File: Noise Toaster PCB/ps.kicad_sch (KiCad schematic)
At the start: 8 parts

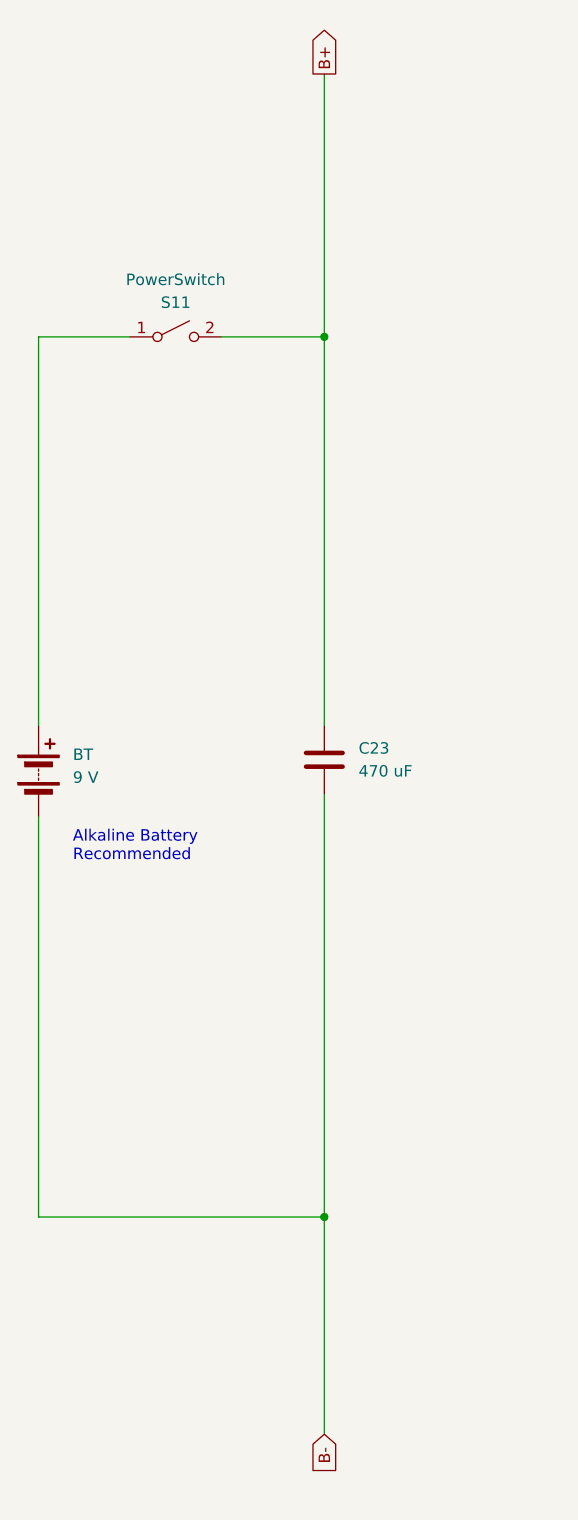
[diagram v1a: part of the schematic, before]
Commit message: refactored the schematic
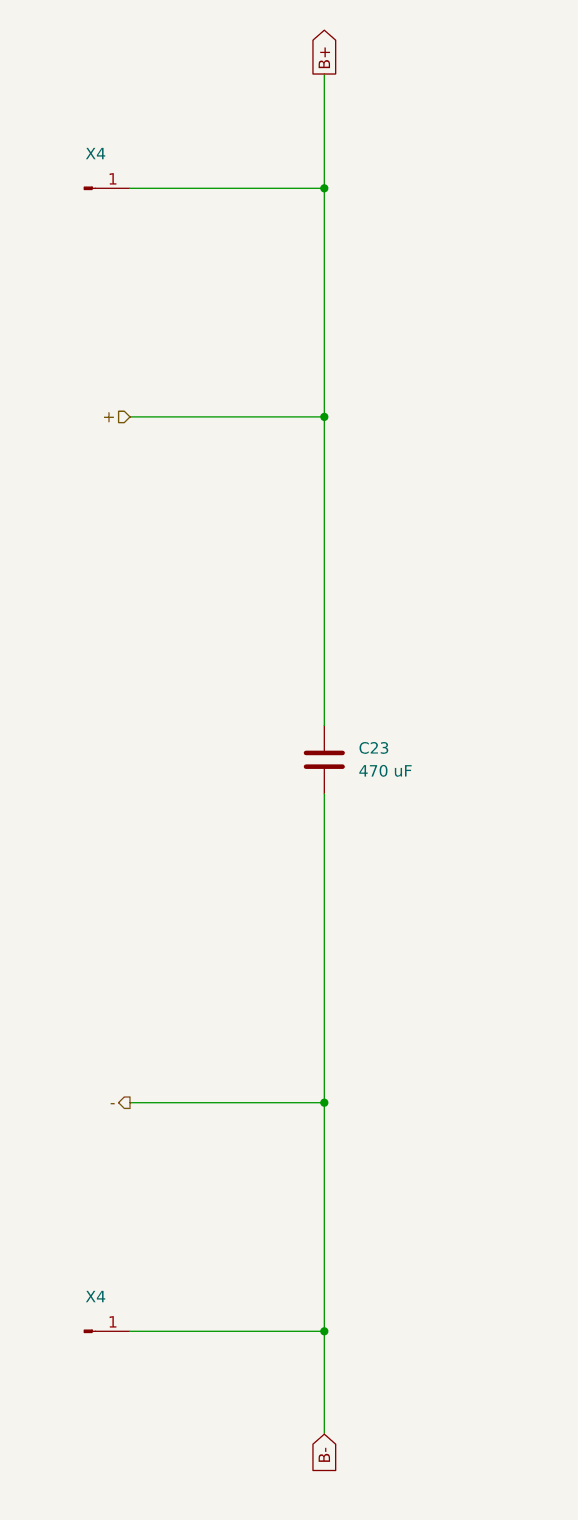
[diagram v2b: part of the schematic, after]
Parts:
- removed BT: 9 V, symbol Device:Battery
- removed PowerSwitch: S11, symbol Switch:SW_SPST
- added X4 (x2): ~, symbol Connector:Conn_01x01_Pin
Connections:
- net B+: now also X4.1 (Pin_1)
- net B-: now also X4.1 (Pin_1)
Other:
- note removed: "Alkaline Battery Recommended"
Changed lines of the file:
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@@
     (comment 3 "Music From Outer Space LLC")
   )
-  (junction (at 59.69 54.61) (diameter 0) (color 0 0 0 0)
+  (junction (at 59.69 139.7) (diameter 0) (color 0 0 0 0)
+  )
+  (junction (at 59.69 165.1) (diameter 0) (color 0 0 0 0)
   )
   (junction (at 160.02 105.41) (diameter 0) (color 0 0 0 0)
@@
   (junction (at 160.02 63.5) (diameter 0) (color 0 0 0 0)
   )
-  (junction (at 59.69 152.4) (diameter 0) (color 0 0 0 0)
+  (junction (at 59.69 63.5) (diameter 0) (color 0 0 0 0)
+  )
+  (junction (at 59.69 38.1) (diameter 0) (color 0 0 0 0)
   )
   (junction (at 105.41 104.14) (diameter 0) (color 0 0 0 0)
   )
-  (wire (pts (xy 59.69 152.4) (xy 59.69 176.53))
+  (wire (pts (xy 38.1 139.7) (xy 59.69 139.7))
+    (stroke (width 0) (type default))
+  )
+  (wire (pts (xy 59.69 38.1) (xy 59.69 63.5))
+    (stroke (width 0) (type default))
+  )
+  (wire (pts (xy 59.69 105.41) (xy 59.69 139.7))
+    (stroke (width 0) (type default))
+  )
+  (wire (pts (xy 38.1 38.1) (xy 59.69 38.1))
     (stroke (width 0) (type default))
   )
@@
     (stroke (width 0) (type default))
   )
-  (wire (pts (xy 27.94 54.61) (xy 27.94 97.79))
-    (stroke (width 0) (type default))
-  )
   (wire (pts (xy 223.52 76.2) (xy 223.52 63.5))
     (stroke (width 0) (type default))
@@
     (stroke (width 0) (type default))
   )
+  (wire (pts (xy 38.1 63.5) (xy 59.69 63.5))
+    (stroke (width 0) (type default))
+  )
   (wire (pts (xy 160.02 26.67) (xy 160.02 41.91))
     (stroke (width 0) (type default))
   )
+  (wire (pts (xy 59.69 63.5) (xy 59.69 97.79))
+    (stroke (width 0) (type default))
+  )
   (wire (pts (xy 105.41 83.82) (xy 105.41 104.14))
     (stroke (width 0) (type default))
@@
     (stroke (width 0) (type default))
   )
-  (wire (pts (xy 27.94 54.61) (xy 38.1 54.61))
-    (stroke (width 0) (type default))
-  )
-  (wire (pts (xy 59.69 54.61) (xy 59.69 97.79))
+  (wire (pts (xy 59.69 165.1) (xy 59.69 176.53))
     (stroke (width 0) (type default))
   )
@@
     (stroke (width 0) (type default))
   )
+  (wire (pts (xy 59.69 139.7) (xy 59.69 165.1))
+    (stroke (width 0) (type default))
+  )
   (wire (pts (xy 120.65 106.68) (xy 120.65 104.14))
     (stroke (width 0) (type default))
@@
     (stroke (width 0) (type default))
   )
-  (wire (pts (xy 27.94 107.95) (xy 27.94 152.4))
-    (stroke (width 0) (type default))
-  )
   (wire (pts (xy 160.02 63.5) (xy 160.02 105.41))
     (stroke (width 0) (type default))
   )
-  (wire (pts (xy 27.94 152.4) (xy 59.69 152.4))
-    (stroke (width 0) (type default))
-  )
-  (wire (pts (xy 59.69 25.4) (xy 59.69 54.61))
+  (wire (pts (xy 38.1 165.1) (xy 59.69 165.1))
+    (stroke (width 0) (type default))
+  )
+  (wire (pts (xy 59.69 25.4) (xy 59.69 38.1))
     (stroke (width 0) (type default))
   )
@@
     (stroke (width 0) (type default))
   )
-  (wire (pts (xy 59.69 152.4) (xy 59.69 105.41))
-    (stroke (width 0) (type default))
-  )
   (wire (pts (xy 105.41 104.14) (xy 120.65 104.14))
-    (stroke (width 0) (type default))
-  )
-  (wire (pts (xy 48.26 54.61) (xy 59.69 54.61))
     (stroke (width 0) (type default))
   )
   (text "Current Drain is\nbetween 15 to \n20 mA. More if\nused at high\noutput levels."
     (at 180.34 88.9 0)
-    (effects (font (size 1.27 1.27)) (justify left bottom))
-  )
-  (text "Alkaline Battery\nRecommended" (at 31.75 113.03 0)
     (effects (font (size 1.27 1.27)) (justify left bottom))
   )
@@
     )
   )
-  (symbol (lib_id "Switch:SW_SPST") (at 43.18 54.61 0) (unit 1)
-    (in_bom yes) (on_board yes) (dnp no) (fields_autoplaced)
-    (property "Reference" "PowerSwitch" (at 43.18 48.26 0)
-      (effects (font (size 1.27 1.27)))
-    )
-    (property "Value" "S11" (at 43.18 50.8 0)
-      (effects (font (size 1.27 1.27)))
-    )
-    (property "Footprint" "" (at 43.18 54.61 0)
-      (effects (font (size 1.27 1.27)) hide)
-    )
-    (property "Datasheet" "~" (at 43.18 54.61 0)
-      (effects (font (size 1.27 1.27)) hide)
-    )
-    (pin "1")
-    (pin "2")
-    (instances
-      (project "Noise Toaster PCB"
-        (path "/7be3f398-d902-4566-9ee4-0bff072cd47e/8163954c-0389-42ef-b929-449d078595e3"
-          (reference "PowerSwitch") (unit 1)
+  (hierarchical_label "-" (shape output) (at 38.1 139.7 180) (fields_autoplaced)
+    (effects (font (size 1.27 1.27)) (justify right))
+  )
+  (hierarchical_label "+" (shape input) (at 38.1 63.5 180) (fields_autoplaced)
+    (effects (font (size 1.27 1.27)) (justify right))
+  )
+  (symbol (lib_id "Connector:Conn_01x01_Pin") (at 33.02 38.1 0) (unit 1)
+    (in_bom yes) (on_board yes) (dnp no)
+    (property "Reference" "X4" (at 34.29 34.29 0)
+      (effects (font (size 1.27 1.27)))
+    )
+    (property "Value" "~" (at 33.655 35.56 0)
+      (effects (font (size 1.27 1.27)))
+    )
+    (property "Footprint" "" (at 33.02 38.1 0)
+      (effects (font (size 1.27 1.27)) hide)
+    )
+    (property "Datasheet" "~" (at 33.02 38.1 0)
+      (effects (font (size 1.27 1.27)) hide)
+    )
+    (pin "1")
+    (instances
+      (project "Noise Toaster PCB"
+        (path "/7be3f398-d902-4566-9ee4-0bff072cd47e/818b46cb-815d-4132-b52d-9731333b7f1f"
+          (reference "X4") (unit 1)
+        )
+        (path "/7be3f398-d902-4566-9ee4-0bff072cd47e/d0369b76-3398-4137-86ba-22490a5aca99"
+          (reference "X21") (unit 1)
+        )
+        (path "/7be3f398-d902-4566-9ee4-0bff072cd47e/0647ade8-e724-4924-aa52-6cbb42374298"
+          (reference "X21") (unit 1)
+        )
+        (path "/7be3f398-d902-4566-9ee4-0bff072cd47e/8163954c-0389-42ef-b929-449d078595e3"
+          (reference "B+") (unit 1)
+        )
+      )
+    )
+  )
+  (symbol (lib_id "Connector:Conn_01x01_Pin") (at 33.02 165.1 0) (unit 1)
+    (in_bom yes) (on_board yes) (dnp no)
+    (property "Reference" "X4" (at 34.29 161.29 0)
+      (effects (font (size 1.27 1.27)))
+    )
+    (property "Value" "~" (at 33.655 162.56 0)
+      (effects (font (size 1.27 1.27)))
+    )
+    (property "Footprint" "" (at 33.02 165.1 0)
+      (effects (font (size 1.27 1.27)) hide)
+    )
+    (property "Datasheet" "~" (at 33.02 165.1 0)
+      (effects (font (size 1.27 1.27)) hide)
+    )
+    (pin "1")
+    (instances
+      (project "Noise Toaster PCB"
+        (path "/7be3f398-d902-4566-9ee4-0bff072cd47e/818b46cb-815d-4132-b52d-9731333b7f1f"
+          (reference "X4") (unit 1)
+        )
+        (path "/7be3f398-d902-4566-9ee4-0bff072cd47e/d0369b76-3398-4137-86ba-22490a5aca99"
+          (reference "X21") (unit 1)
+        )
+        (path "/7be3f398-d902-4566-9ee4-0bff072cd47e/0647ade8-e724-4924-aa52-6cbb42374298"
+          (reference "X21") (unit 1)
+        )
+        (path "/7be3f398-d902-4566-9ee4-0bff072cd47e/8163954c-0389-42ef-b929-449d078595e3"
+          (reference "B-") (unit 1)
         )
       )
@@
         )
       )
-    )
-  )
-  (symbol (lib_id "Device:Battery") (at 27.94 102.87 0) (unit 1)
-    (in_bom yes) (on_board yes) (dnp no) (fields_autoplaced)
-    (property "Reference" "BT" (at 31.75 101.0285 0)
-      (effects (font (size 1.27 1.27)) (justify left))
-    )
-    (property "Value" "9 V" (at 31.75 103.5685 0)
-      (effects (font (size 1.27 1.27)) (justify left))
-    )
-    (property "Footprint" "" (at 27.94 101.346 90)
-      (effects (font (size 1.27 1.27)) hide)
-    )
-    (property "Datasheet" "~" (at 27.94 101.346 90)
-      (effects (font (size 1.27 1.27)) hide)
-    )
-    (pin "1")
-    (pin "2")
-    (instances
-      (project "Noise Toaster PCB"
-        (path "/7be3f398-d902-4566-9ee4-0bff072cd47e/8163954c-0389-42ef-b929-449d078595e3"
-          (reference "BT") (unit 1)
-        )
-      )

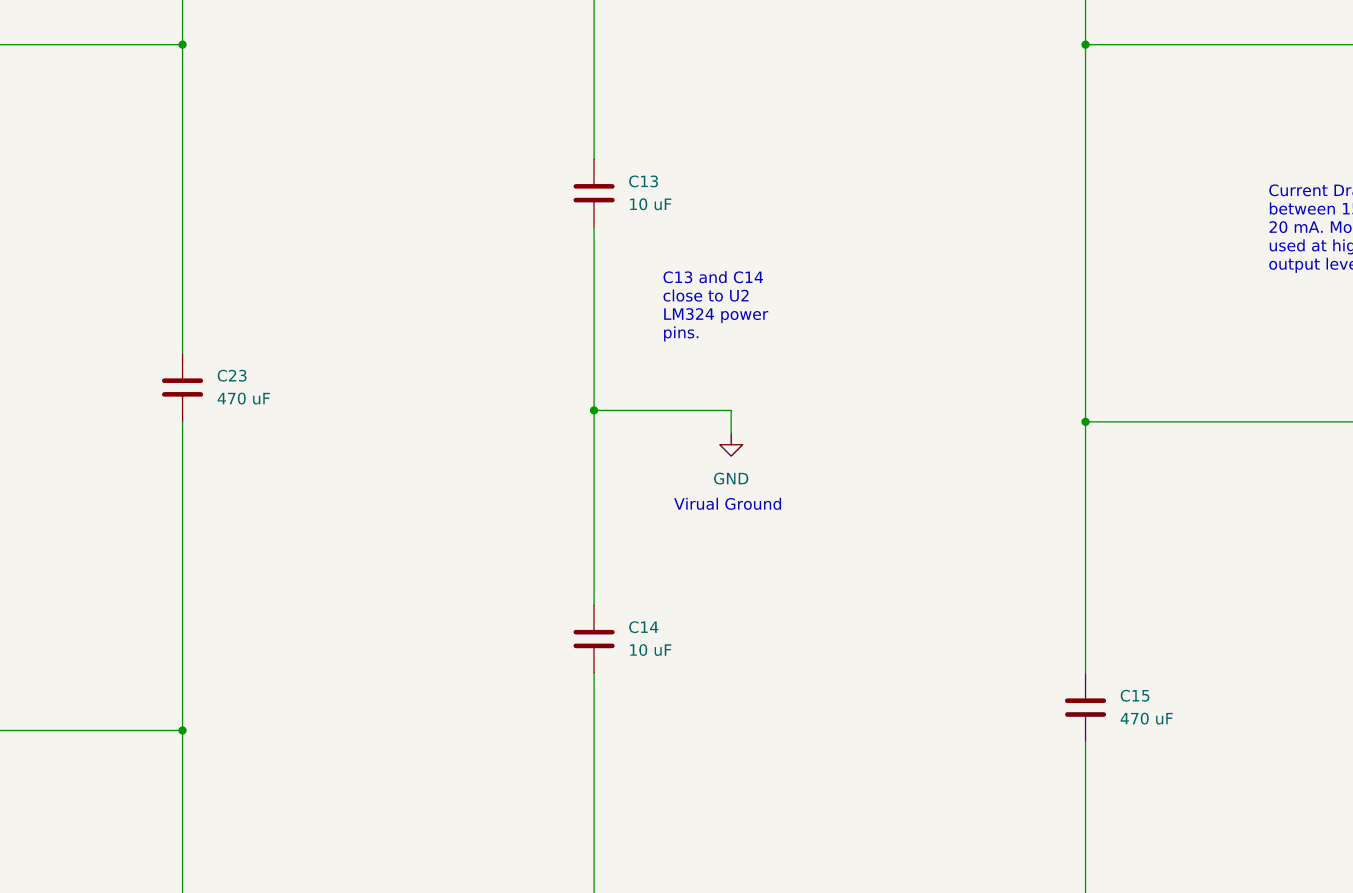
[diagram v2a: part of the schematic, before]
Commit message: wireing and components have been checked
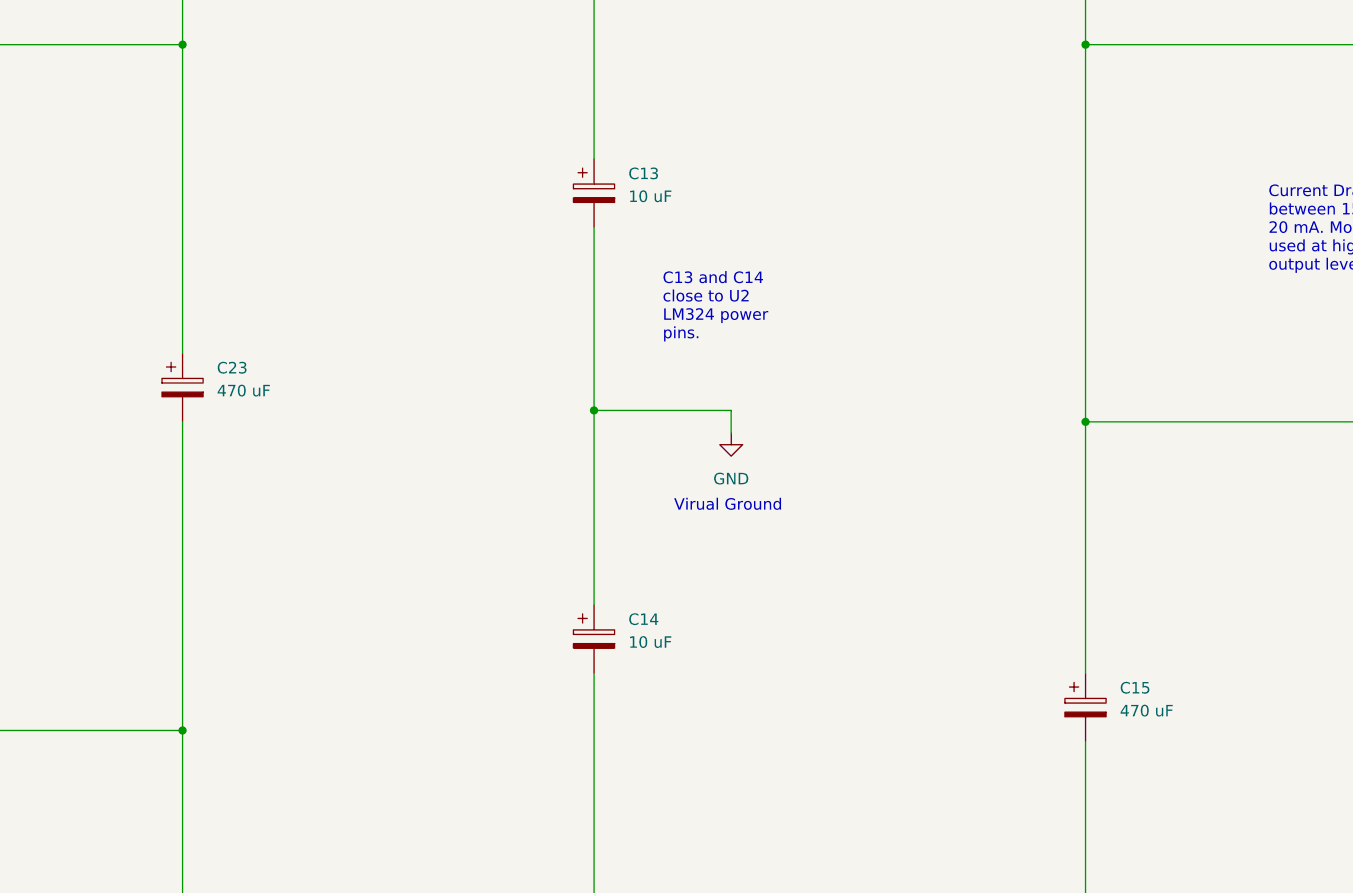
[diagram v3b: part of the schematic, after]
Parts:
- removed C13, C14: 10 uF, symbol Device:C
- removed C15, C23: 470 uF, symbol Device:C
- added C13, C14: 10 uF, symbol Device:C_Polarized
- added C15, C23: 470 uF, symbol Device:C_Polarized
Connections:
- net B+: now also C13.1, C23.1
- net B-: now also C14.2, C15.2, C23.2
- net GND: now also C13.2, C14.1, C15.1
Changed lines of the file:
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@@
     )
   )
-  (symbol (lib_id "Device:C") (at 105.41 80.01 0) (unit 1)
+  (symbol (lib_id "Device:C_Polarized") (at 59.69 101.6 0) (unit 1)
     (in_bom yes) (on_board yes) (dnp no) (fields_autoplaced)
-    (property "Reference" "C13" (at 109.22 78.74 0)
+    (property "Reference" "C23" (at 63.5 99.441 0)
       (effects (font (size 1.27 1.27)) (justify left))
     )
-    (property "Value" "10 uF" (at 109.22 81.28 0)
+    (property "Value" "470 uF" (at 63.5 101.981 0)
       (effects (font (size 1.27 1.27)) (justify left))
     )
-    (property "Footprint" "" (at 106.3752 83.82 0)
+    (property "Footprint" "" (at 60.6552 105.41 0)
       (effects (font (size 1.27 1.27)) hide)
     )
-    (property "Datasheet" "~" (at 105.41 80.01 0)
+    (property "Datasheet" "~" (at 59.69 101.6 0)
       (effects (font (size 1.27 1.27)) hide)
     )
@@
       (project "Noise Toaster PCB"
         (path "/7be3f398-d902-4566-9ee4-0bff072cd47e/8163954c-0389-42ef-b929-449d078595e3"
-          (reference "C13") (unit 1)
+          (reference "C23") (unit 1)
+        )
+      )
+    )
+  )
+  (symbol (lib_id "Device:C_Polarized") (at 160.02 137.16 0) (unit 1)
+    (in_bom yes) (on_board yes) (dnp no) (fields_autoplaced)
+    (property "Reference" "C15" (at 163.83 135.001 0)
+      (effects (font (size 1.27 1.27)) (justify left))
+    )
+    (property "Value" "470 uF" (at 163.83 137.541 0)
+      (effects (font (size 1.27 1.27)) (justify left))
+    )
+    (property "Footprint" "" (at 160.9852 140.97 0)
+      (effects (font (size 1.27 1.27)) hide)
+    )
+    (property "Datasheet" "~" (at 160.02 137.16 0)
+      (effects (font (size 1.27 1.27)) hide)
+    )
+    (pin "1")
+    (pin "2")
+    (instances
+      (project "Noise Toaster PCB"
+        (path "/7be3f398-d902-4566-9ee4-0bff072cd47e/8163954c-0389-42ef-b929-449d078595e3"
+          (reference "C15") (unit 1)
         )
       )
@@
     )
   )
-  (symbol (lib_id "Device:C") (at 105.41 129.54 0) (unit 1)
+  (symbol (lib_id "Device:C_Polarized") (at 105.41 80.01 0) (unit 1)
     (in_bom yes) (on_board yes) (dnp no) (fields_autoplaced)
-    (property "Reference" "C14" (at 109.22 128.27 0)
+    (property "Reference" "C13" (at 109.22 77.851 0)
       (effects (font (size 1.27 1.27)) (justify left))
     )
-    (property "Value" "10 uF" (at 109.22 130.81 0)
+    (property "Value" "10 uF" (at 109.22 80.391 0)
       (effects (font (size 1.27 1.27)) (justify left))
     )
-    (property "Footprint" "" (at 106.3752 133.35 0)
+    (property "Footprint" "" (at 106.3752 83.82 0)
       (effects (font (size 1.27 1.27)) hide)
     )
-    (property "Datasheet" "~" (at 105.41 129.54 0)
+    (property "Datasheet" "~" (at 105.41 80.01 0)
       (effects (font (size 1.27 1.27)) hide)
     )
@@
       (project "Noise Toaster PCB"
         (path "/7be3f398-d902-4566-9ee4-0bff072cd47e/8163954c-0389-42ef-b929-449d078595e3"
-          (reference "C14") (unit 1)
-        )
-      )
-    )
-  )
-  (symbol (lib_id "Device:C") (at 59.69 101.6 0) (unit 1)
-    (in_bom yes) (on_board yes) (dnp no) (fields_autoplaced)
-    (property "Reference" "C23" (at 63.5 100.33 0)
-      (effects (font (size 1.27 1.27)) (justify left))
-    )
-    (property "Value" "470 uF" (at 63.5 102.87 0)
-      (effects (font (size 1.27 1.27)) (justify left))
-    )
-    (property "Footprint" "" (at 60.6552 105.41 0)
-      (effects (font (size 1.27 1.27)) hide)
-    )
-    (property "Datasheet" "~" (at 59.69 101.6 0)
-      (effects (font (size 1.27 1.27)) hide)
-    )
-    (pin "1")
-    (pin "2")
-    (instances
-      (project "Noise Toaster PCB"
-        (path "/7be3f398-d902-4566-9ee4-0bff072cd47e/8163954c-0389-42ef-b929-449d078595e3"
-          (reference "C23") (unit 1)
-        )
-      )
-    )
-  )
-  (symbol (lib_id "Device:C") (at 160.02 137.16 0) (unit 1)
-    (in_bom yes) (on_board yes) (dnp no) (fields_autoplaced)
-    (property "Reference" "C15" (at 163.83 135.89 0)
-      (effects (font (size 1.27 1.27)) (justify left))
-    )
-    (property "Value" "470 uF" (at 163.83 138.43 0)
-      (effects (font (size 1.27 1.27)) (justify left))
-    )
-    (property "Footprint" "" (at 160.9852 140.97 0)
-      (effects (font (size 1.27 1.27)) hide)
-    )
-    (property "Datasheet" "~" (at 160.02 137.16 0)
-      (effects (font (size 1.27 1.27)) hide)
-    )
-    (pin "1")
-    (pin "2")
-    (instances
-      (project "Noise Toaster PCB"
-        (path "/7be3f398-d902-4566-9ee4-0bff072cd47e/8163954c-0389-42ef-b929-449d078595e3"
-          (reference "C15") (unit 1)
+          (reference "C13") (unit 1)
         )
       )
@@
         )
       )
+    )
+  )
+  (symbol (lib_id "Device:C_Polarized") (at 105.41 129.54 0) (unit 1)
+    (in_bom yes) (on_board yes) (dnp no) (fields_autoplaced)
+    (property "Reference" "C14" (at 109.22 127.381 0)
+      (effects (font (size 1.27 1.27)) (justify left))
+    )
+    (property "Value" "10 uF" (at 109.22 129.921 0)
+      (effects (font (size 1.27 1.27)) (justify left))
+    )
+    (property "Footprint" "" (at 106.3752 133.35 0)
+      (effects (font (size 1.27 1.27)) hide)
+    )
+    (property "Datasheet" "~" (at 105.41 129.54 0)
+      (effects (font (size 1.27 1.27)) hide)
+    )
+    (pin "1")
+    (pin "2")
+    (instances
+      (project "Noise Toaster PCB"
+        (path "/7be3f398-d902-4566-9ee4-0bff072cd47e/8163954c-0389-42ef-b929-449d078595e3"
+          (reference "C14") (unit 1)
+        )
+      )
